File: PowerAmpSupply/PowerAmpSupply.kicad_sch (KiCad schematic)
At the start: 1 part, among them U1 LM5123-Q1

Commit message: PowerAmpSupply schematic progress
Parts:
- added C1: 0pF, Capacitor_SMD:C_0603_1608Metric, symbol Device:C_Small
- added C10, C3: 0.1µF 100V, Capacitor_SMD:C_0603_1608Metric, symbol Device:C_Small
- added C11: 4.7µF, Capacitor_SMD:C_0805_2012Metric, symbol Device:C
- added C12: 10µF, Capacitor_SMD:C_0805_2012Metric, symbol Device:C
- added C13: 470pF, Capacitor_SMD:C_0603_1608Metric, symbol Device:C
- added C14: 0.47µF, Capacitor_SMD:C_0603_1608Metric, symbol Device:C
- added C15: 33pF, Capacitor_SMD:C_0603_1608Metric, symbol Device:C_Small
- added C16: 1.5nF, Capacitor_SMD:C_0603_1608Metric, symbol Device:C_Small
- added C17, C18, C19, C20, C21, C24, C25, C26, C27, C28: 10µF 100V x2, Capacitor_SMD:C_1210_3225Metric, symbol Device:C
- added C2: 0.1µF, Capacitor_SMD:C_0603_1608Metric, symbol Device:C_Small
- added C22, C23: 560µF 63V, Capacitor_THT:CP_Radial_D12.5mm_P5.00mm, symbol Device:C_Polarized
- added C4: 0.1µF 100V, Capacitor_SMD:C_0603_1608Metric, symbol Device:C
- added C5: 2.2µF 100V, Capacitor_SMD:C_0805_2012Metric, symbol Device:C
- added C6, C7: 22µF 25V, Capacitor_SMD:C_1210_3225Metric, symbol Device:C
- added C8, C9: 1µF 50Vl, Capacitor_SMD:C_0805_2012Metric, symbol Device:C
- added D1: MBR12U100L, Package_TO_SOT_SMD:TO-277B, symbol Device:D_Schottky_AAK
- added FB1, FB2: Shunt?, Inductor_SMD:L_0603_1608Metric, symbol Device:FerriteBead_Small
- added JP1: VH/CP, Jumper:SolderJumper-3_P1.3mm_Open_RoundedPad1.0x1.5mm, symbol Jumper:SolderJumper_3_Open
- added L1: 1.5µH, BW_PassiveMechanical:L_Vishay_IHLP-6767, symbol Device:L_Ferrite
- added Q1, Q3: GAN3R2-100CBE, BW_Active:WLCSP-8-SOT8072, symbol BW_Active:GAN3R2-100CBE
- added Q2, Q4: PNP, Package_TO_SOT_SMD:SOT-23, symbol Device:Q_PNP_BEC
- added R1: 1.5mΩ 3W, Resistor_SMD:R_2512_6332Metric, symbol Device:R_US
- added R10: 33kΩ, Resistor_SMD:R_0603_1608Metric, symbol Device:R_US
- added R11: 21kΩ, Resistor_SMD:R_0603_1608Metric, symbol Device:R_US
- added R2: 0Ω, Resistor_SMD:R_0603_1608Metric, symbol Device:R_Small_US
- added R3: 76.8kΩ, Resistor_SMD:R_0603_1608Metric, symbol Device:R_Small_US
- added R4: 0Ω, Resistor_SMD:R_0603_1608Metric, symbol Device:R_US
- added R5: 8.87kΩ, Resistor_SMD:R_0603_1608Metric, symbol Device:R_Small_US
- added R6, R8: 3.3Ω, Resistor_SMD:R_0603_1608Metric, symbol Device:R_Small_US
- added R7: 1kΩ, Resistor_SMD:R_0603_1608Metric, symbol Device:R_US
- added R9: 220kΩ, Resistor_SMD:R_0603_1608Metric, symbol Device:R_Small_US
- added TP1: SW, TestPoint:TestPoint_Pad_D1.5mm, symbol Connector:TestPoint_Small
- added TP2: HO, TestPoint:TestPoint_Pad_D1.5mm, symbol Connector:TestPoint_Small
- added TP3: LO, TestPoint:TestPoint_Pad_D1.5mm, symbol Connector:TestPoint_Small
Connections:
- net VIN: now reaches U1.1 (CSP)
- net VIN: now also U1.8 (BIAS), C1.1, C6.1, C7.1, C8.1, C9.1, R1.1, R3.1
- net GND: now reaches U1.10 (PGND)
- net GND: now also U1.19 (AGND), U1.21 (EP), C10.1, C11.2, C12.2, C13.2, C14.2, C15.2, C16.2, C17.2, C18.2, C19.2, C2.2, C20.2, C21.2, C22.2, C23.2, C24.2, C25.2, C26.2, C27.2, C28.2, C4.2, C5.2, C6.2, C7.2, C8.2, C9.2, JP1.1 (A), Q3.2 (S), Q3.4 (S), Q3.6 (S), Q3.8 (S), Q4.3 (C), R10.2, R11.2, R5.2
- net at U1.11 (LO): now also Q4.1 (B), R8.1
- net at U1.12 (MODE): now also U1.9 (VCC), C11.1, JP1.3 (B)
- net at U1.13 (UVLO/EN): now also R4.2
- net at U1.14 (SYNC/DITHER/VH/CP): now also JP1.2 (C)
- net at U1.15 (RT): now also R11.1
- net at U1.16 (VREF/RANGE): now also C13.1, R10.1
- net at U1.17 (SS): now also C14.1
- net at U1.18 (TRK): now also C12.1, R7.2
- net at U1.2 (CSN): now also C1.2, R2.1
- net at U1.20 (COMP): now also C15.1, R9.1
- net VOUT: now reaches U1.3 (VOUT/SENSE)
- net VOUT: now also C10.2, C17.1, C18.1, C19.1, C20.1, C21.1, C22.1, C23.1, C24.1, C25.1, C26.1, C27.1, C28.1, C4.1, C5.1, D1.3 (K), Q1.3 (D), Q1.5 (D), Q1.7 (D)
- net PGOOD: now reaches U1.4 (PGOOD)
- net at U1.5 (HO): now also Q2.1 (B), R6.1
- net at U1.6 (SW): now also C3.2, D1.1 (A), D1.2 (A), L1.2, Q1.2 (S), Q1.4 (S), Q1.6 (S), Q1.8 (S), Q2.3 (C), Q3.3 (D), Q3.5 (D), Q3.7 (D), TP1.1
- net at U1.7 (HB): now also C3.1
- new net: FB1.1, Q1.1 (G), TP2.1
- new net: FB1.2, Q2.2 (E), R6.2
- new net: FB2.1, Q4.2 (E), R8.2
- new net: C16.1, R9.2
- new net: L1.1, R1.2, R2.2
- new net: C2.1, R3.2, R4.1, R5.1
- new net: FB2.2, Q3.1 (G), TP3.1
- new net VTRK: R7.1
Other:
- note added: "More CIN?"
- note added: "switch snubber?"
- moved on the sheet: U1

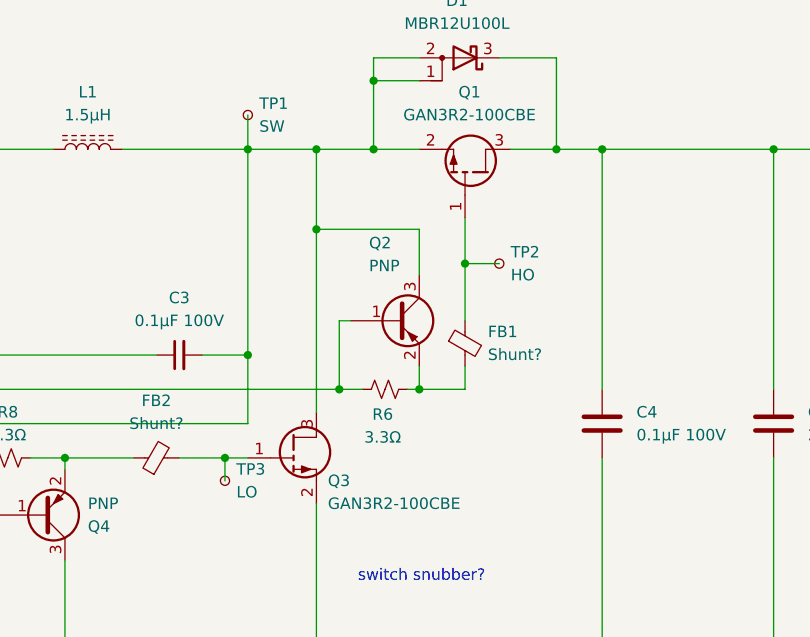
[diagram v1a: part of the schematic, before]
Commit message: CleanLVSupply reduce -17V switch frequency
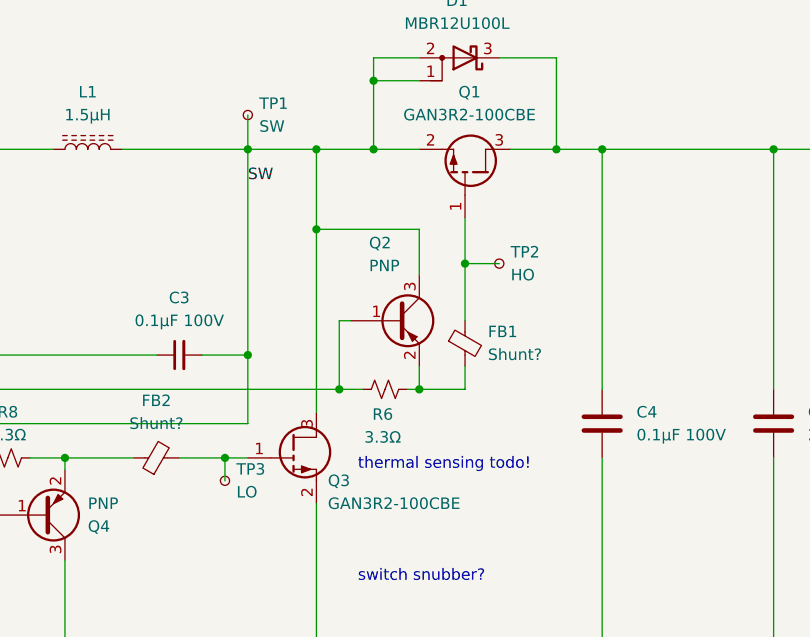
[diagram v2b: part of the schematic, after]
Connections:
- net SW: now reaches C3.2, D1.1 (A), D1.2 (A), L1.2, Q1.2 (S), Q1.4 (S), Q1.6 (S), Q1.8 (S), Q2.3 (C), Q3.3 (D), Q3.5 (D), Q3.7 (D), TP1.1, U1.6 (SW)
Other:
- note added: "thermal sensing todo!"
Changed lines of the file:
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@@
+		)
+	)
+	(text "thermal sensing todo!"
+		(exclude_from_sim no)
+		(at 344.424 143.002 0)
+		(effects
+			(font
+				(size 1.27 1.27)
+			)
 		)
 	)
@@
 		)
 	)
+	(label "SW"
+		(at 322.58 111.76 0)
+		(fields_autoplaced yes)
+		(effects
+			(font
+				(size 1.27 1.27)
+			)
+			(justify left bottom)
+		)
+	)

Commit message: PowerAmplifier initially complete, PowerAmpSupply progress
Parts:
- removed R7: 1kΩ, Resistor_SMD:R_0603_1608Metric, symbol Device:R_US
- added C16: ?pF 100+V, Capacitor_SMD:C_0603_1608Metric, symbol Device:C_Small
- added C30: 22pF, Capacitor_SMD:C_0603_1608Metric, symbol Device:C_Small
- added C31: 10µF 25V, Capacitor_SMD:C_0805_2012Metric, symbol Device:C
- added C32: 2.2µF 100Vl, Capacitor_SMD:C_1206_3216Metric, symbol Device:C
- added C33: 0.1µF 100V, Capacitor_SMD:C_0603_1608Metric, symbol Device:C
- added C34: 10µF 50V, Capacitor_SMD:C_1206_3216Metric, symbol Device:C
- added C35: 0.1µF, Capacitor_SMD:C_0603_1608Metric, symbol Device:C_Small
- added J1: VTRK_EXT, Connector_PinHeader_2.54mm:PinHeader_1x01_P2.54mm_Vertical, symbol Connector:Conn_01x01_Pin
- added M1: 12V 6Vstart <100mA, BW_Connectors:Amphenol_MINITEK_0.8_2P_V, symbol Motor:Fan
- added R13, R14: 28kΩ 0.1%, Resistor_SMD:R_0603_1608Metric, symbol Device:R_US
- added R15: 10.5kΩ 0.1%, Resistor_SMD:R_0603_1608Metric, symbol Device:R_US
- added R16: 110kΩ, Resistor_SMD:R_0603_1608Metric, symbol Device:R_Small_US
- added R17: 13kΩ, Resistor_SMD:R_0603_1608Metric, symbol Device:R_Small_US
- added R18: 10kΩ, Resistor_SMD:R_0603_1608Metric, symbol Device:R_Small_US
- added R19, R20: 0Ω, Resistor_SMD:R_0603_1608Metric, symbol Device:R_Small_US
- added R8, R9: ?Ω, Resistor_SMD:R_1206_3216Metric, symbol Device:R_Small_US
- added TH1: 10kΩ 3950B, Resistor_SMD:R_0603_1608Metric, symbol Device:Thermistor_NTC_US
- added U2: NCP51460, Package_TO_SOT_SMD:SOT-23, symbol BW_Active:NCP51460
- added U3: AP2202-ADJ, Package_TO_SOT_SMD:SOT-23-5, symbol BW_Active:LDO_ADJ
- added U4: TPSM365R3, BW_Active:TI_QFN-FCMOD-HR, symbol BW_Active:TPSM365R3/6
- C11: value 4.7µF -> 4.7µF 25Vl
- C12: value 10µF -> 4.7µF; footprint Capacitor_SMD:C_0805_2012Metric -> Capacitor_SMD:C_0603_1608Metric
- C23: renamed from C22; value 560µF 63V -> 1mF 80V; footprint Capacitor_THT:CP_Radial_D12.5mm_P5.00mm -> Capacitor_THT:CP_Radial_D16.0mm_P7.50mm
- C24: renamed from C23; value 560µF 63V -> 1mF 80V; footprint Capacitor_THT:CP_Radial_D12.5mm_P5.00mm -> Capacitor_THT:CP_Radial_D16.0mm_P7.50mm
- Q1, Q3: value GAN3R2-100CBE -> EPC2306; footprint BW_Active:WLCSP-8-SOT8072 -> BW_Active:EPC2306; symbol BW_Active:GAN3R2-100CBE -> BW_Active:EPC2306
- R6: value 3.3Ω -> 1Ω
- R7: renamed from R8; value 3.3Ω -> 1Ω
- renumbered C16 to C17, C17 to C18, C18 to C19, C19 to C20, C20 to C21, C21 to C22, C24 to C25, C25 to C26, C26 to C27, C27 to C28, C28 to C29, R9 to R10, R10 to R11, R11 to R12
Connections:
- net GND: now also C16.1, C32.2, C33.2, C34.2, C35.2, M1.2 (-), R15.2, R18.2, R20.2, TH1.2, U2.3 (GND), U3.2 (GND), U4.10 (GND), U4.11 (RT/MODE/SYNC); no longer Q3.8 (S)
- net SW: now also R8.2; no longer Q1.8 (S)
- net VOUT: now also C32.1, C33.1, U4.2 (EN), U4.3 (VIN)
- net VTRK: now also C12.1, U1.18 (TRK), R13.2, R14.2, R15.1
- net EN: now reaches C2.1, R3.2, R4.1, R5.1
- new net: R17.2, R19.1, U3.4 (ADJ)
- new net: C31.1, M1.1 (+), R17.1, U3.5 (OUT)
- new net: R13.1, U2.2 (OUT)
- new net: U4.5 (SW), U4.6 (SW)
- new net: C35.1, U4.8 (VCC)
- new net: C30.2, R16.2, R18.1, U4.9 (FB/BIAS)
- new net: C31.2, R20.1
- new net: R19.2, TH1.1
- new net: J1.1 (Pin_1), R14.1
- new net: R8.1, R9.2
- new net: C16.2, R9.1
- new net +12V: C30.1, C34.1, R16.1, U2.1 (IN), U3.1 (IN), U3.3 (EN), U4.4 (VOUT)
- no-connect marks 0 -> 3
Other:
- note added: "V_ADJ = 1.25V Start (6V) at thermistor ~3.4k = 50°C Max (12V) at thermistor ~1.5k = 72°C Increase bottom series resistor to shift temps up"
- note removed: "switch snubber?"
- note removed: "thermal sensing todo!"
- moved on the sheet: C1, C10, C11, C12, C13, C14, C15, C17, C18, C19, C2, C20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

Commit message: PowerAmpSupply FET change and layout progress
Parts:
- added C1: 0.1µF, Capacitor_SMD:C_0603_1608Metric, symbol Device:C_Small
- C12: renamed from C11; value 4.7µF 25Vl -> 4.7µF; footprint Capacitor_SMD:C_0805_2012Metric -> Capacitor_SMD:C_0603_1608Metric
- FB1, FB2: footprint Inductor_SMD:L_0603_1608Metric -> Inductor_SMD:L_0402_1005Metric_Pad0.77x0.64mm_HandSolder
- Q2, Q4: footprint Package_TO_SOT_SMD:SOT-23 -> Package_SON:HUSON-3-1EP_2x2mm_P1.3mm_EP1.1x1.6mm
- renumbered C9 to C10, C10 to C11, C12 to C13, C13 to C14, C14 to C15, C15 to C16, C16 to C17, C17 to C18, C18 to C19, C1 to C2, C19 to C20, C20 to C21, C21 to C22, C22 to C23, C23 to C24, C24 to C25, C25 to C26, C26 to C27, C27 to C28, C28 to C29, C2 to C3, C29 to C30, C30 to C31, C31 to C32, C32 to C33, C33 to C34, C34 to C35, C35 to C36, C3 to C4, C4 to C5, C5 to C6, C6 to C7, C7 to C8, C8 to C9
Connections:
- net GND: now also C1.1
- net VIN: now also C1.2
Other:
- moved on the sheet: C12, C3, JP1, R3, R4, R5

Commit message: PowerAmpSupply almost done
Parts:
- added C25, C34: 10µF 100V x2, Capacitor_SMD:C_1210_3225Metric, symbol Device:C
- added C28: 1mF 80V, Capacitor_THT:CP_Radial_D16.0mm_P7.50mm, symbol Device:C_Polarized
- added C7: 1mF 35V, Capacitor_THT:CP_Radial_D10.0mm_P5.00mm, symbol Device:C_Polarized
- added J1, J2: VIN_BRIDGE, BW_PassiveMechanical:HolePad_2.5mm_3.5mm, symbol Connector:Conn_01x01_Socket
- added J3, J4: GND_BRIDGE, BW_PassiveMechanical:HolePad_2.5mm_3.5mm, symbol Connector:Conn_01x01_Socket
- added J5: VOUT, BW_Connectors:TE_644749-2, symbol Connector:Conn_01x02_Pin
- added J6: VIN, BW_Connectors:TE_2042274_Solder, symbol Connector:Conn_01x05_Pin
- added R1: 3mΩ 2W, Resistor_SMD:R_0612_1632Metric, symbol Device:R_US
- M1: footprint BW_Connectors:Amphenol_MINITEK_0.8_2P_V -> BW_Connectors:Amphenol_MINITEK_0.8_2P_V_BoardEdge
- R18: renamed from R17; value 13kΩ -> 23.2kΩ
- R2: renamed from R1; value 1.5mΩ 3W -> 3mΩ 2W; footprint Resistor_SMD:R_2512_6332Metric -> Resistor_SMD:R_0612_1632Metric
- TH1: value 10kΩ 3950B -> 10kΩ 4250B; footprint Resistor_SMD:R_0603_1608Metric -> Resistor_SMD:R_0402_1005Metric_Pad0.72x0.64mm_HandSolder
- renumbered C9 to C10, C10 to C11, C11 to C13, C13 to C14, C14 to C15, C15 to C16, C16 to C17, C17 to C18, C18 to C19, C19 to C20, C20 to C21, C21 to C22, C22 to C23, C23 to C24, C24 to C26, C25 to C27, C26 to C29, C4 to C3, C27 to C30, C28 to C31, C29 to C32, C30 to C33, C31 to C35, C32 to C36, C33 to C37, C34 to C38, C35 to C39, C3 to C4, C36 to C40, C7 to C8, C8 to C9, J1 to J7, R9 to R10, R10 to R11, R11 to R12, R12 to R13, R13 to R14, R14 to R15, R15 to R16, R16 to R17, R18 to R19, R19 to R20, R20 to R21, R2 to R3, R3 to R4, R4 to R5, R5 to R6, R6 to R7, R7 to R8, R8 to R9
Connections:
- net GND: now also C25.2, C28.2, C34.2, C7.2, J3.1 (Pin_1), J4.1 (Pin_1), J5.2 (Pin_2), J6.1 (Pin_1), J6.3 (Pin_3), J6.4 (Pin_4)
- net VIN: now also C7.1, J1.1 (Pin_1), J2.1 (Pin_1), J6.2 (Pin_2), R1.1
- net VOUT: now also C25.1, C28.1, C34.1, J5.1 (Pin_1)
- net at L1.1, R2.2, R3.2: now also R1.2
- no-connect marks 3 -> 4
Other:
- note added: "1.1V - 3.3V"
- note added: "V_ADJ = 1.25V Start (6V) at thermistor ~6.1k = 36°C Max (12V) at thermistor ~2.7k = 55°C Increase bottom series resistor to shift temps up"
- note removed: "More CIN?"
- note removed: "V_ADJ = 1.25V Start (6V) at thermistor ~3.4k = 50°C Max (12V) at thermistor ~1.5k = 72°C Increase bottom series resistor to shift temps up"
- moved on the sheet: C1, C10, C11, C12, C13, C14, C15, C16, C17, C18, C19, C2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

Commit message: PowerAmp+Supply additions
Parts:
- added D2: PGOOD, LED_SMD:LED_0805_2012Metric, symbol Device:LED
- added F1: Fuse, symbol Device:Fuse
- added R14: 13.3kΩ, Resistor_SMD:R_0603_1608Metric, symbol Device:R_US
- C18, C2, R10, R9: now not fitted
- renumbered J6 to J5, J5 to J6, R14 to R15, R15 to R16, R16 to R17, R17 to R18, R18 to R19, R19 to R20, R20 to R21, R21 to R22
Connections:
- net GND: now also D2.1 (K)
- net PGOOD: now also D2.2 (A), R14.2
- net VOUT: now also F1.1; no longer J6.1 (Pin_1)
- new net VOUT_FUSED: F1.2, J6.1 (Pin_1), R14.1
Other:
- note added: "Tracking voltage 1.1V - 3.3V VOUT = 16.364 * VTRK_EXT"
- note removed: "1.1V - 3.3V"
- moved on the sheet: J6

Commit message: PowerAmpSupply final + ICL, PowerAmp final
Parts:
- F1: value Fuse -> 6.3A; footprint (none) -> BW_PassiveMechanical:Fuse_Schurter_MSB
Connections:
- net VIN: no longer J5.2 (Pin_2)
- new net Inrush Limit/IN: J5.2 (Pin_2)
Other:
- added sheet Inrush Limit (inrush.kicad_sch)
- moved on the sheet: D2, F1, J6, R14

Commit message: PowerAmp+Supply fan LDO change, Supply Rgate fix
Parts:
- R7, R8: value 1Ω -> 3.3Ω
- U3: value AP2202-ADJ -> TPS7A2401
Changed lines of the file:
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@@
 			)
 		)
-		(property "Value" "AP2202-ADJ"
+		(property "Value" "TPS7A2401"
 			(at 163.83 225.552 0)
 			(effects
@@
 			)
 		)
-		(property "Value" "1Ω"
+		(property "Value" "3.3Ω"
 			(at 302.26 86.36 90)
 			(effects
@@
 			)
 		)
-		(property "Value" "1Ω"
+		(property "Value" "3.3Ω"
 			(at 343.916 86.614 90)
 			(effects
